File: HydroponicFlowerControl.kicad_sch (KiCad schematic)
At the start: 5 parts

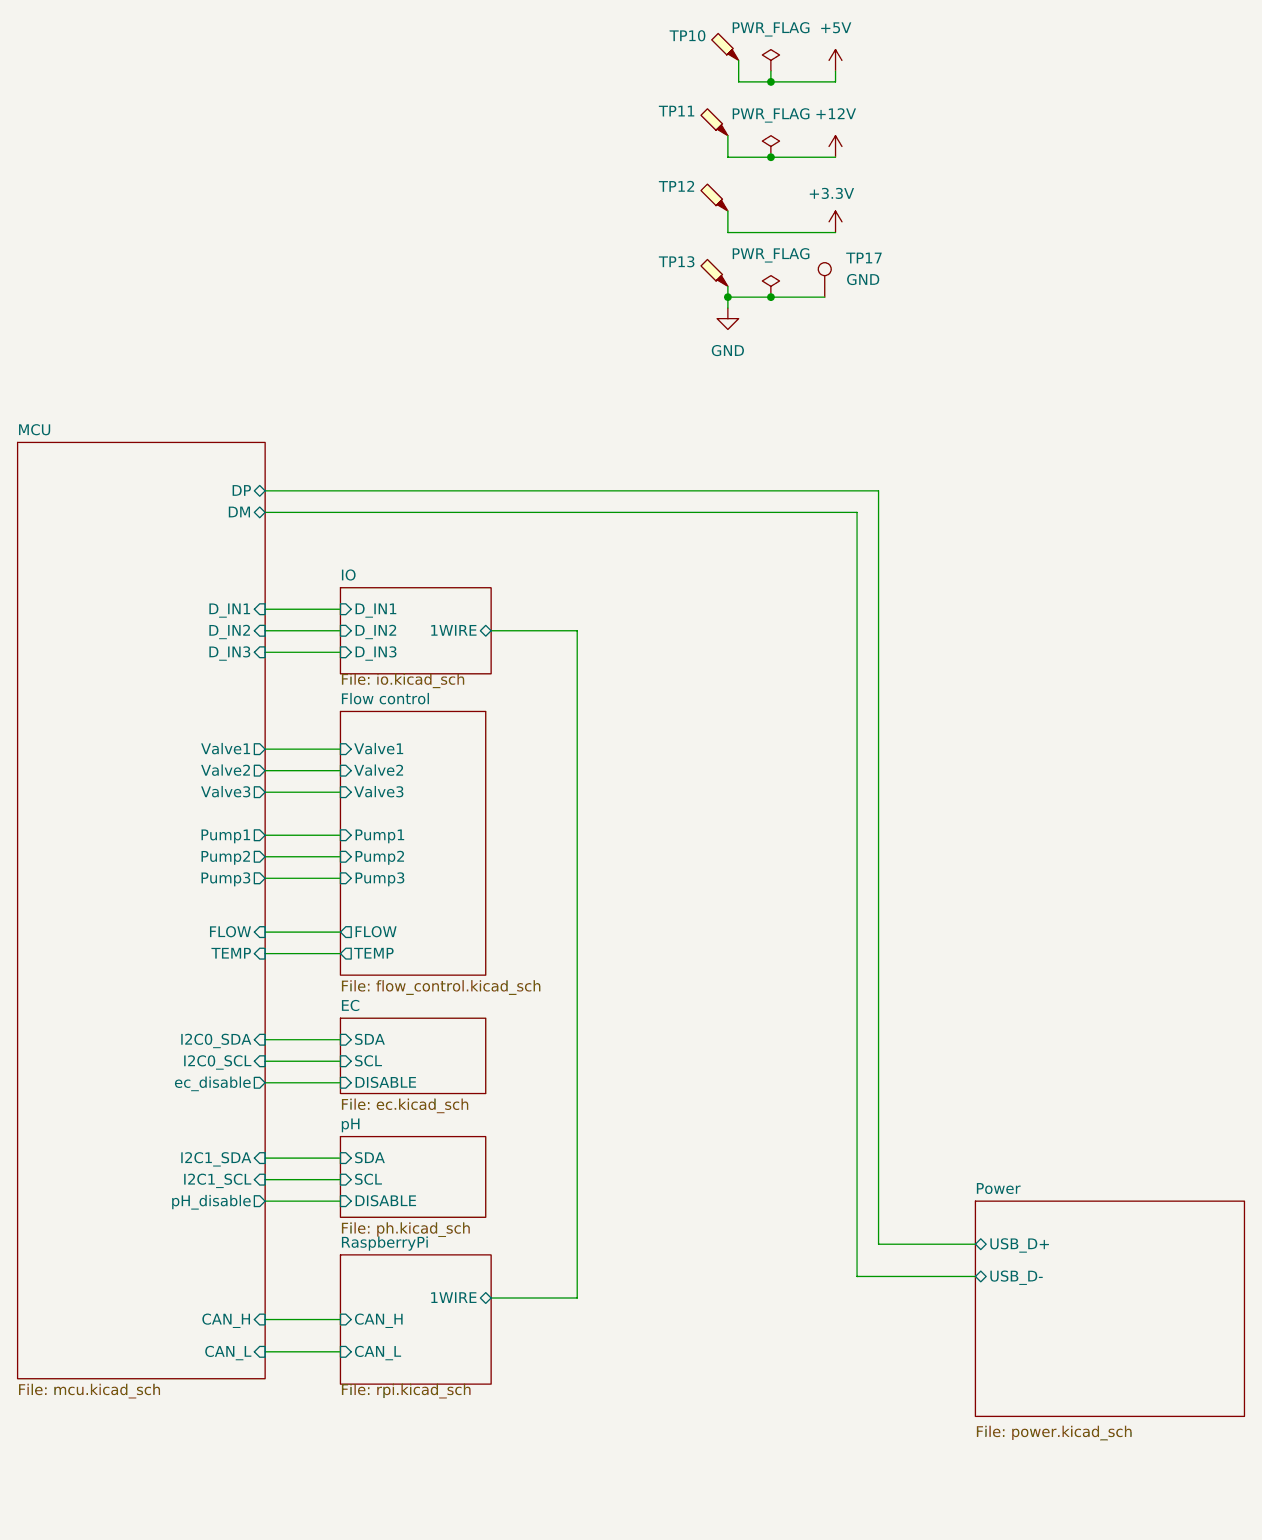
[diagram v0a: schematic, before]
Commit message: Add Reverse polarity protection
Closes #55
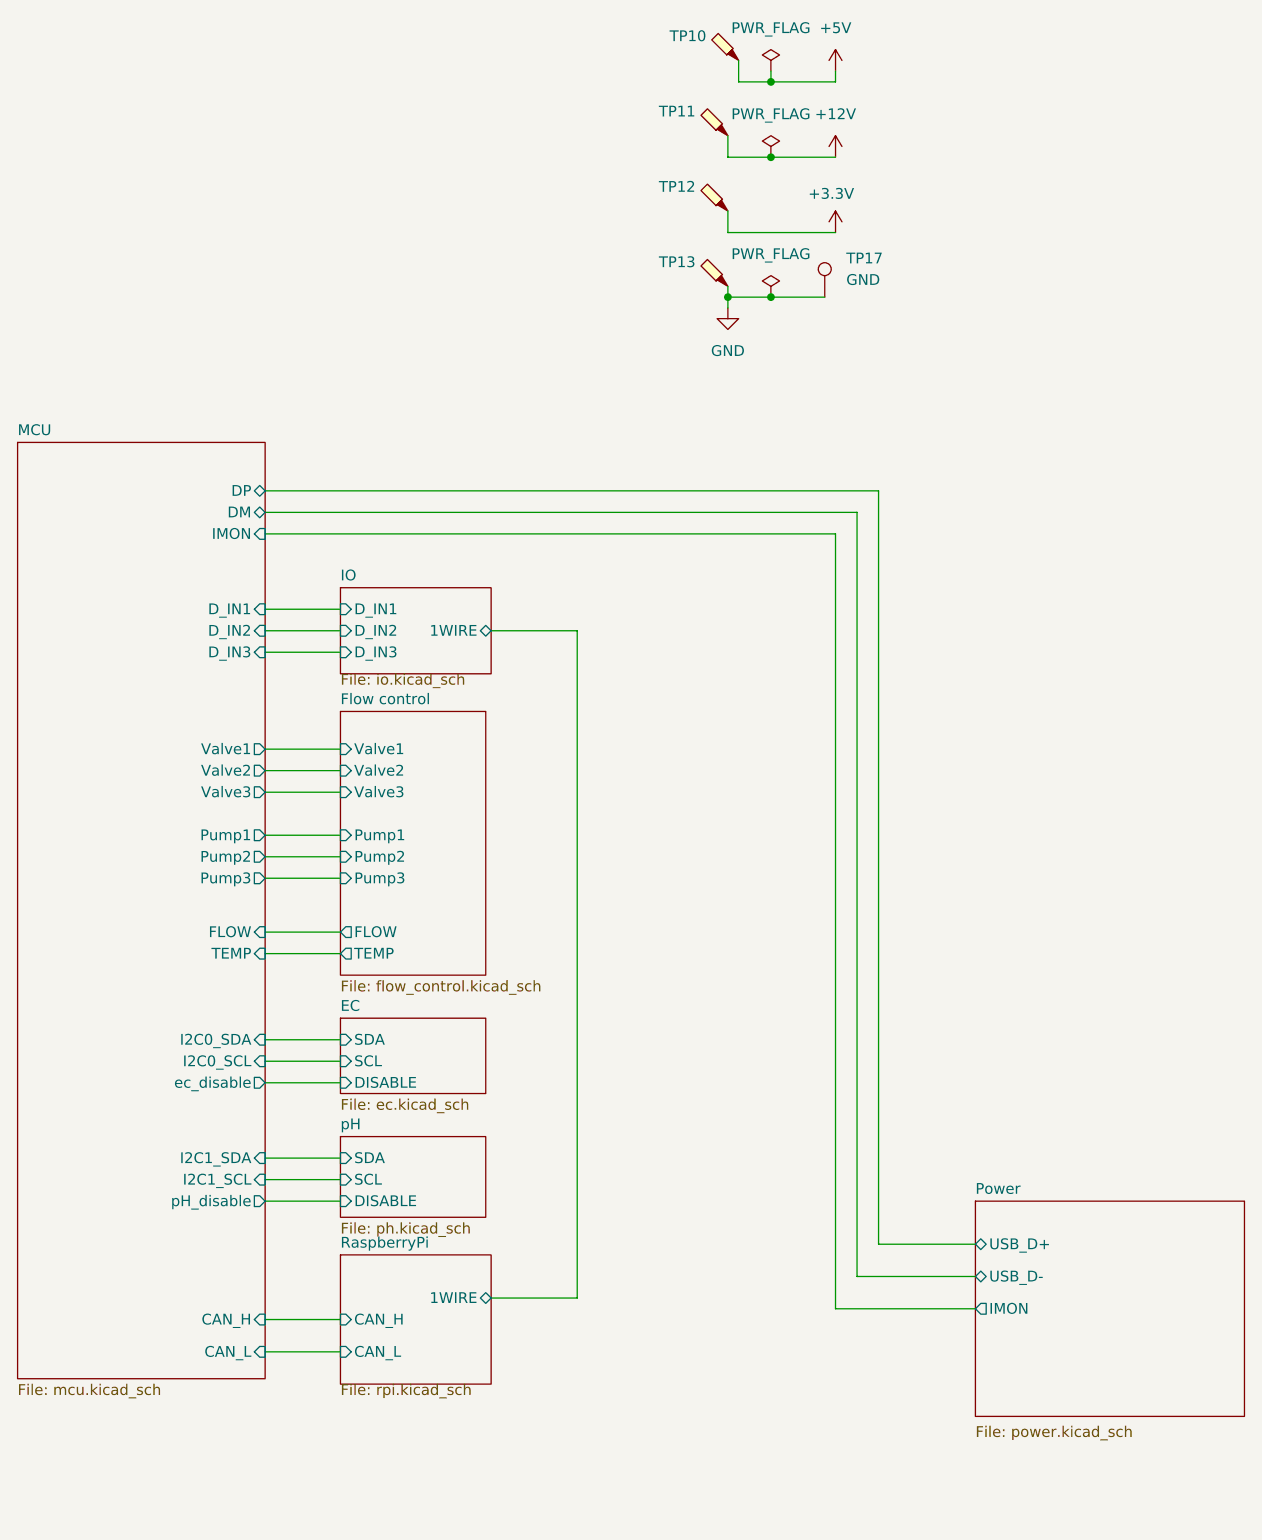
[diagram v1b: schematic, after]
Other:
- sheet MCU ports: added IMON; removed none
- sheet Power ports: added IMON; removed none
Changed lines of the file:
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@@
+	(wire
+		(pts
+			(xy 116.84 168.91) (xy 133.35 168.91)
+		)
+		(stroke
+			(width 0)
+			(type default)
+		)
+	)
 	(wire
 		(pts
@@
 	(wire
 		(pts
+			(xy 116.84 77.47) (xy 116.84 168.91)
+		)
+		(stroke
+			(width 0)
+			(type default)
+		)
+	)
+	(wire
+		(pts
 			(xy 49.53 72.39) (xy 121.92 72.39)
 		)
@@
 		(pts
 			(xy 119.38 74.93) (xy 49.53 74.93)
+		)
+		(stroke
+			(width 0)
+			(type default)
+		)
+	)
+	(wire
+		(pts
+			(xy 49.53 77.47) (xy 116.84 77.47)
 		)
 		(stroke
@@
 			)
 		)
+		(pin "IMON" output
+			(at 133.35 168.91 180)
+			(effects
+				(font
+					(size 1.27 1.27)
+				)
+				(justify left)
+			)
+		)
 		(instances
 			(project "HydroponicFlowerControl"
@@
 			(effects
 				(font
+					(size 1.27 1.27)
+				)
+				(justify right)
+			)
+		)
+		(pin "IMON" input
+			(at 49.53 77.47 0)
+			(effects
+				(font

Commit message: Replace 4 of the 6 highside outputs with TPS4H160B
See #50
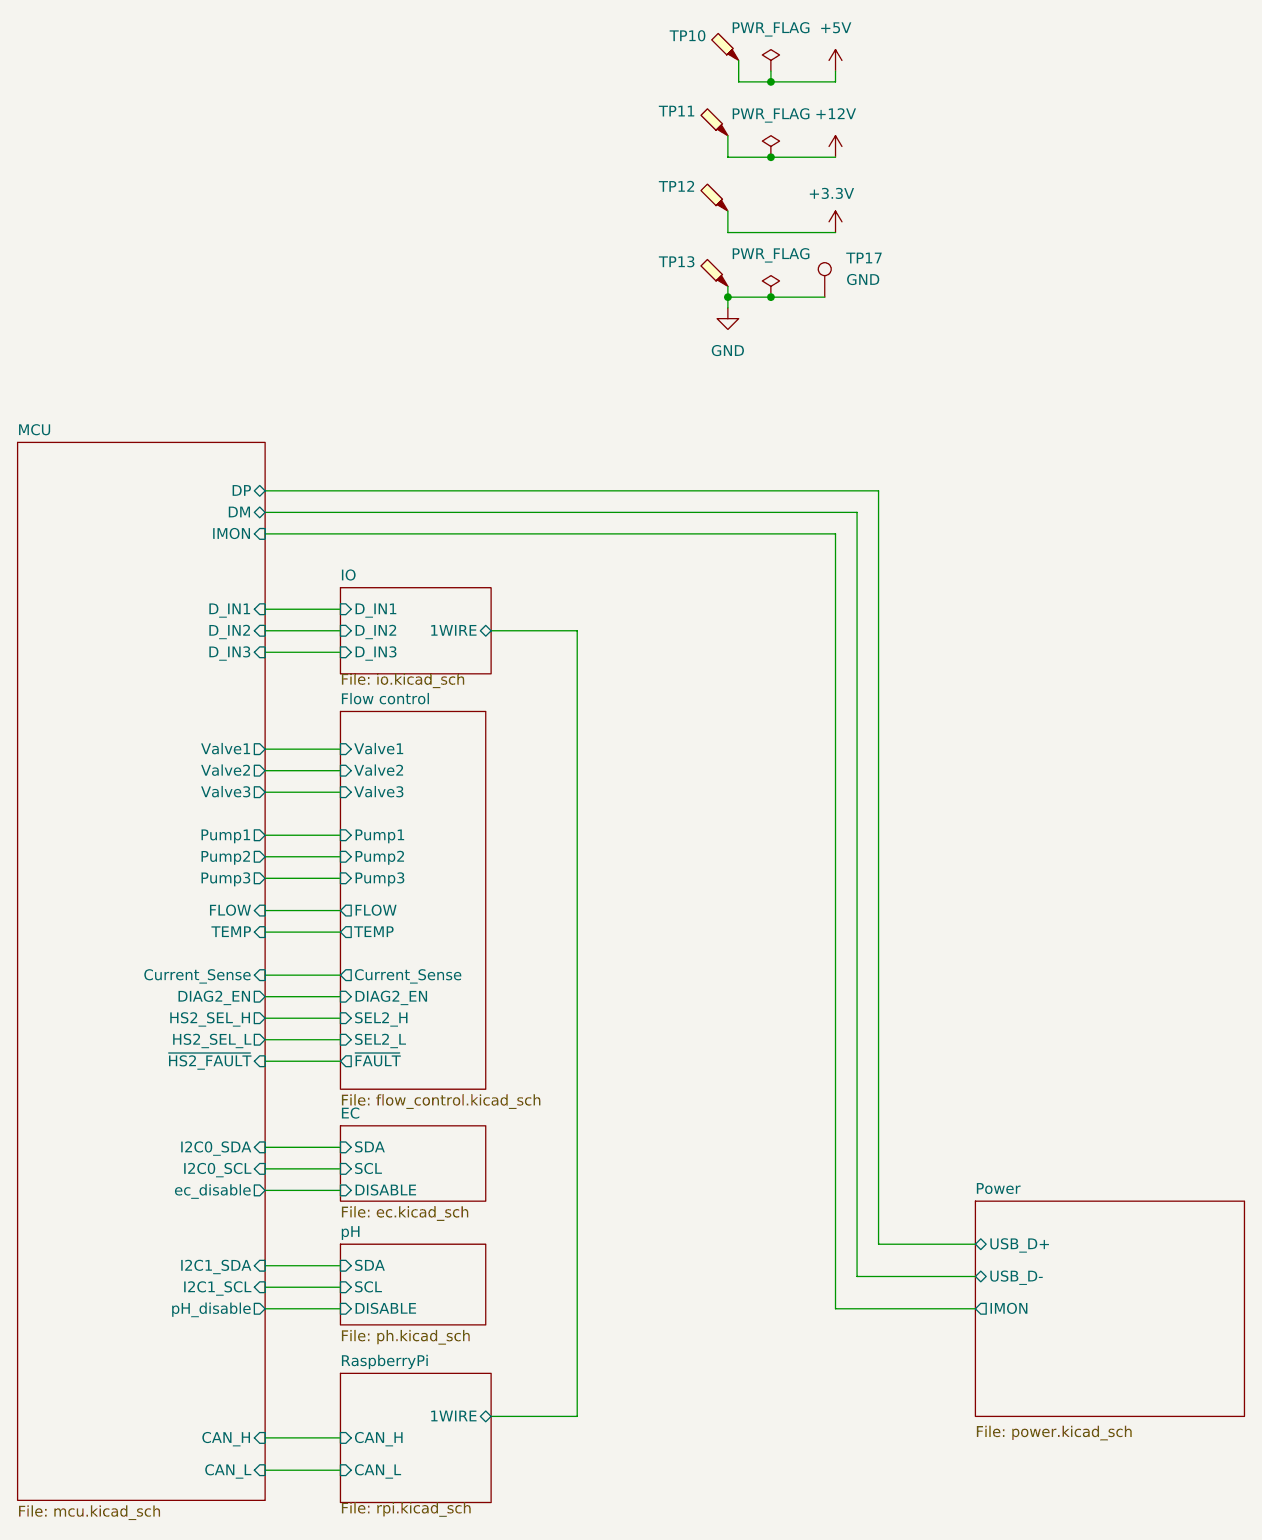
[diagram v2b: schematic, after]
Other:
- sheet Flow control ports: added Current_Sense, DIAG2_EN, SEL2_H, SEL2_L, ~{FAULT}; removed none
- sheet MCU ports: added Current_Sense, DIAG2_EN, HS2_SEL_H, HS2_SEL_L, ~{HS2_FAULT}; removed none

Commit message: Replace the last 2 of the highside outputs with TPS4H160B
Closes #50
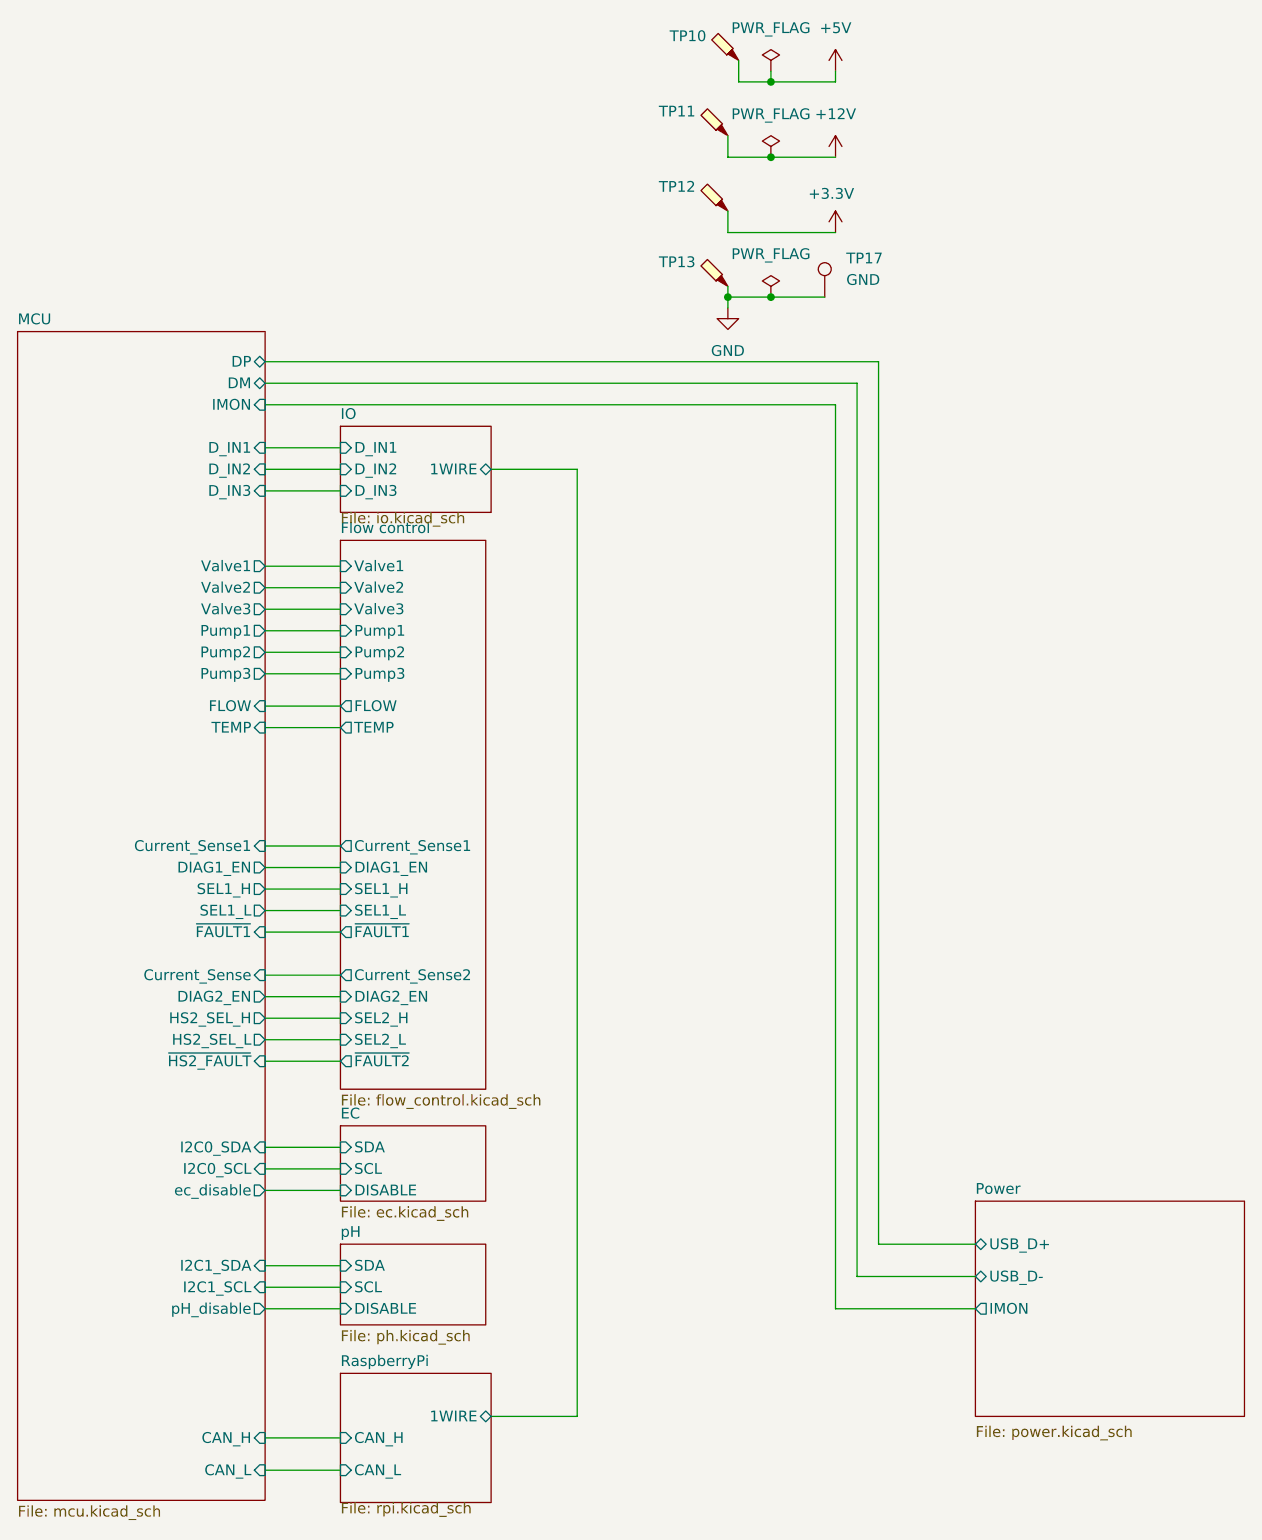
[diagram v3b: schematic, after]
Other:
- sheet Flow control ports: added Current_Sense1, Current_Sense2, DIAG1_EN, SEL1_H, SEL1_L, ~{FAULT1}, ~{FAULT2}; removed Current_Sense, ~{FAULT}
- sheet MCU ports: added Current_Sense1, DIAG1_EN, SEL1_H, SEL1_L, ~{FAULT1}; removed none
